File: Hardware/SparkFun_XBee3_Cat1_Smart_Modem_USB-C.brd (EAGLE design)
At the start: 53.3 x 59.7 mm, 114 parts, among them J1 USB Female Type C Connector, J3 USB Female Type C Connector, J4 QWIIC_RIGHT_ANGLE, U1 FSUSB30MUX_MSOP10, U2 AP63203, U3 ESD Diode, U5 ESD Diode, U6 CP210X

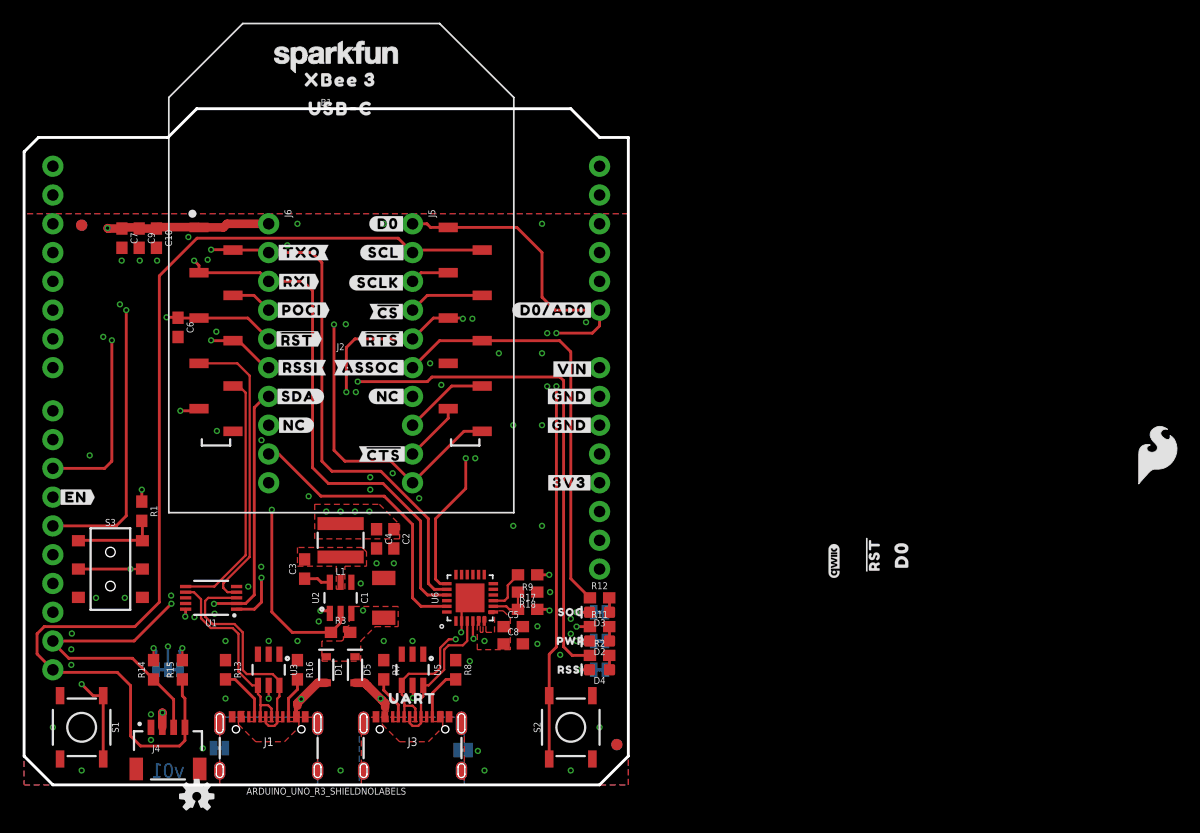
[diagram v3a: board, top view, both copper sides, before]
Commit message: Adds FT231XS, pushes all signals to bottom layer that were on layer two
* Adds decoupling cap and 100 Ohm resistor to UART MUX
* Moves some silk around
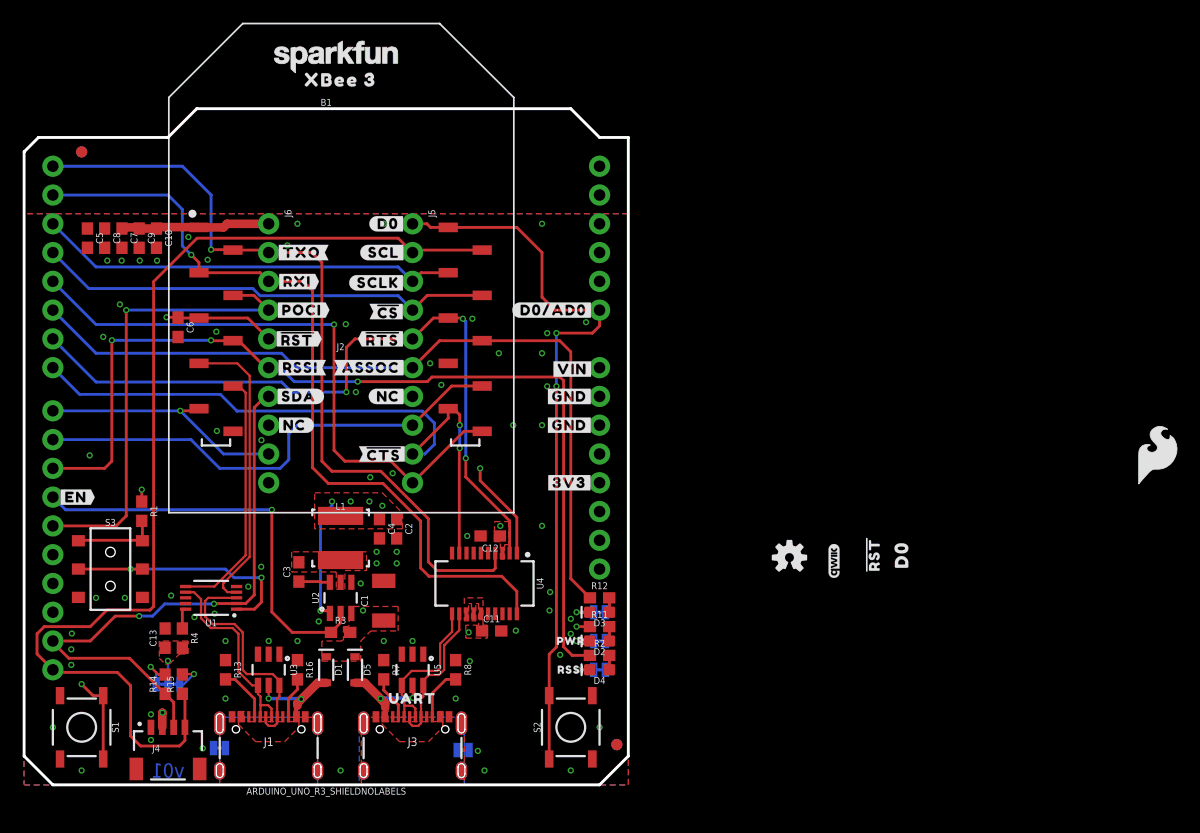
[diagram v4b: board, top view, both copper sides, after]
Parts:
- removed R17: 22k, SparkFun-Resistors:0603
- removed R18: 33k, SparkFun-Resistors:0603
- removed R9: 10k, SparkFun-Resistors:0603
- removed U$24, U$25: (no value), topmirror:USB#C1342
- removed U$3: (no value), topmirror:SOC30
- removed U6: CP210X, SparkFun-IC-Comms:QFN24
- added C11, C12, C13: 0.1uF, SparkFun-Capacitors:0603
- added R4: 100, SparkFun-Resistors:0603
- added U4: FT231XS, SparkFun-IC-Comms:SSOP20_L
- C5: value 0.1uF -> 47pF
- C8: value 4.7uF -> 10pF
- D4: value BLUE -> Yellow
- L1: value 4.7μH -> 3.9UH; device SparkFun-Coils:INDUCTOR_4X4MM -> SparkFun-Coils:INDUCTOR_3.9UH
- R11: value 1k -> 4.7k
- moved LOGO2 56.4 mm to (67.6, 20.1)
- moved C5 50.9 mm to (5.59, 48.3), turned to 270 degrees
- moved C8 50.8 mm to (7.11, 48.3), turned to 270 degrees
- moved U$4 30.8 mm to (35.3, 3.05), turned to 0 degrees
- moved U$51 25.1 mm to (47.2, 10.0)
- moved U$52 25.1 mm to (47.2, 12.7)
- moved U$49 25.1 mm to (47.1, 15.2)
- moved FD1 6.48 mm to (5.08, 55.9)
- moved FD2 6.48 mm to (5.08, 55.9)
- moved U$17 5.08 mm to (17.0, 41.9)
- moved U$38 5.08 mm to (38.6, 26.5)
- moved U$11 5.08 mm to (38.1, 47.0)
- moved U$13 5.08 mm to (17.5, 29.2)
- moved U$14 5.08 mm to (17.1, 36.8)
- moved U$15 5.08 mm to (17.4, 34.3)
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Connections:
- removed net N$9: R9.2, U6.9
- net 3.3V: now also C11.1, C12.1, C13.1, R4.2, U4.13, U4.14, U4.15, U4.3; no longer R9.1, U1.10, U6.5, U6.6, U6.7
- net D+: now also U4.12; no longer U6.3
- net D-: now also U4.11; no longer U6.4
- net D13/TXO: now also U4.4; no longer U6.20
- net D14/RXI: now also U4.20; no longer U6.21
- net D6/!RTS!: now also U4.2; no longer U6.19
- net D7/!CTS!: now also U4.9
- net D8/!DTR!: now also U4.1; no longer U6.23
- net GND: now also C11.2, C12.2, C13.2, U4.16, U4.6; no longer R18.1, U6.2, U6.PAD
- net N$10: now also R4.1, U1.10; no longer R17.1, R18.2, U6.8
- net VIN: no longer R17.2
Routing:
- net D7/!CTS!: track 45.2 -> 58.6 mm, vias 0 -> 2
- net D14/RXI: track 64.4 -> 71.4 mm
- net D13/TXO: track 67.1 -> 71.0 mm
- net N$9: track 3.77 -> 0.00 mm
- net GND: track 3.37 -> 0.00 mm, vias 74 -> 71
- net D6/!RTS!: track 68.5 -> 65.6 mm
- net D8/!DTR!: track 47.6 -> 50.5 mm, vias 1 -> 2
- net 3.3V: track 31.7 -> 29.7 mm, vias 13 -> 11
- net N$10: track 3.81 -> 1.97 mm
- net D-: track 15.6 -> 14.2 mm, vias 2 -> 0
- net D1/SCL: track 97.8 -> 96.4 mm
- net VIN: track 46.1 -> 44.9 mm

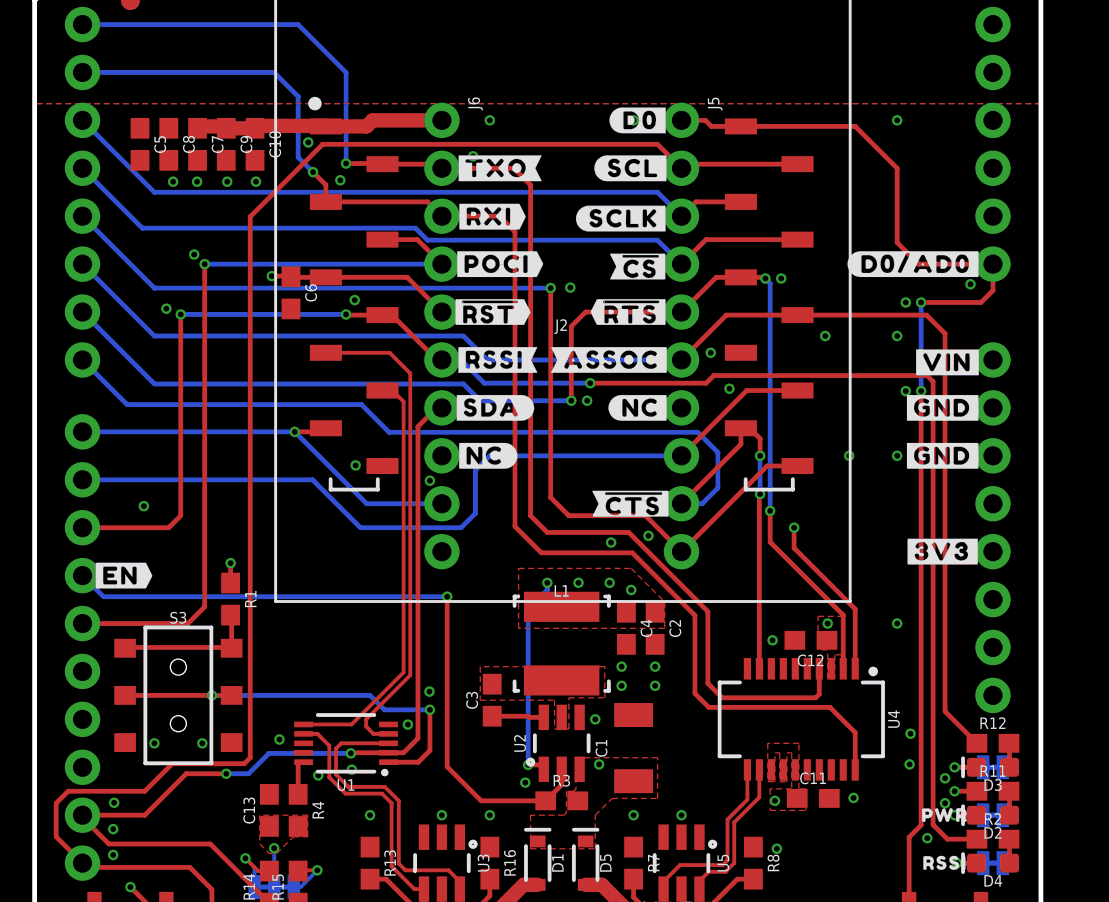
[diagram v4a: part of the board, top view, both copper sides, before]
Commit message: More vias, improves routing
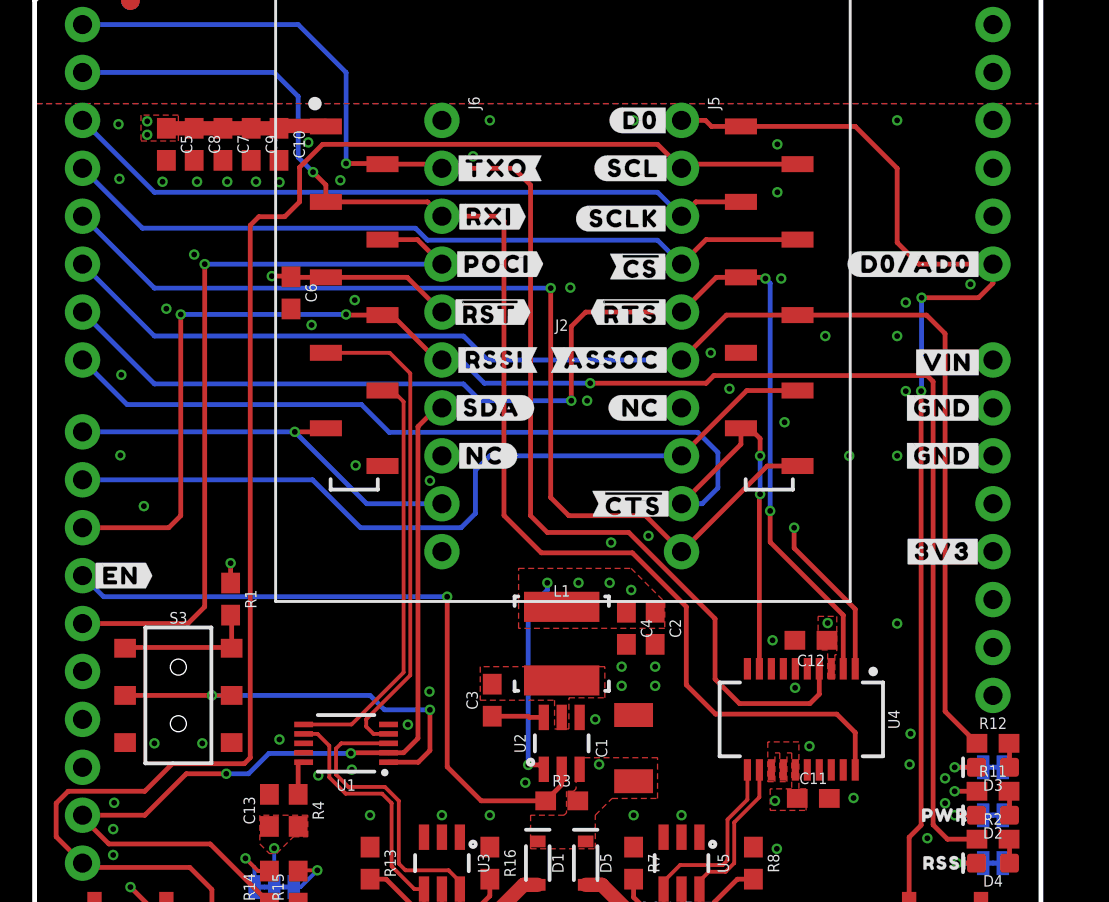
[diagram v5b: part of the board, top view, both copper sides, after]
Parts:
- moved C5 1.40 mm to (6.99, 48.3)
- moved C7 1.35 mm to (9.98, 48.3)
- moved C8 1.35 mm to (8.46, 48.3)
- moved C9 1.32 mm to (11.5, 48.3)
- moved C10 1.27 mm to (13.0, 48.3)
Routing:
- net 3.3V: track 29.7 -> 25.4 mm, vias 11 -> 13
- net D1/SCL: track 96.4 -> 97.2 mm
